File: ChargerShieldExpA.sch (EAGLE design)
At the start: 104 parts, among them IC1 TL431, IC2 LM324N, Q1 BUZ11, Q2 BD648, Q3 BUZ171, Q4 IRFZ48Z, T1 BC548, X1 +Vin, X2 VCC, X3 Battery

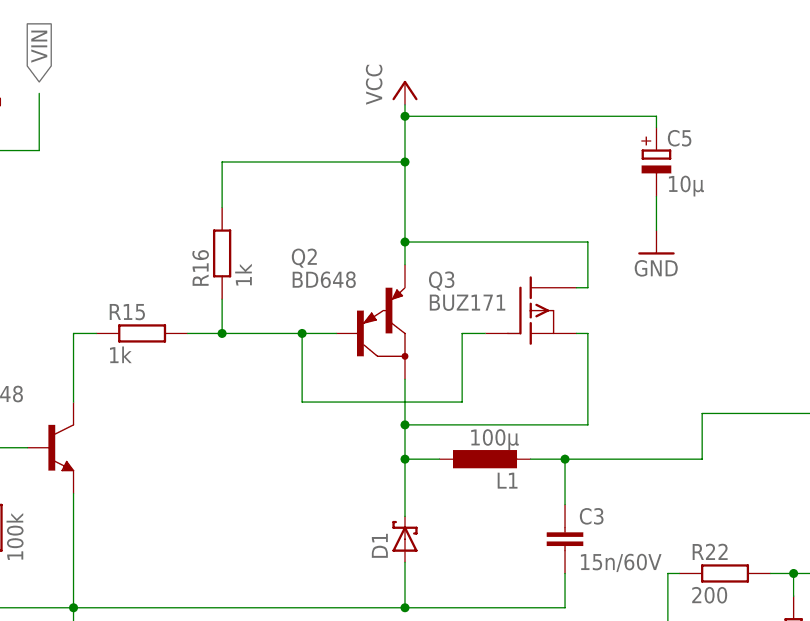
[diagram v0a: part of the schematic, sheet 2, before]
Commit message: - PROTOTYPE_BOARD define for prototype board use. - wrong FET connections
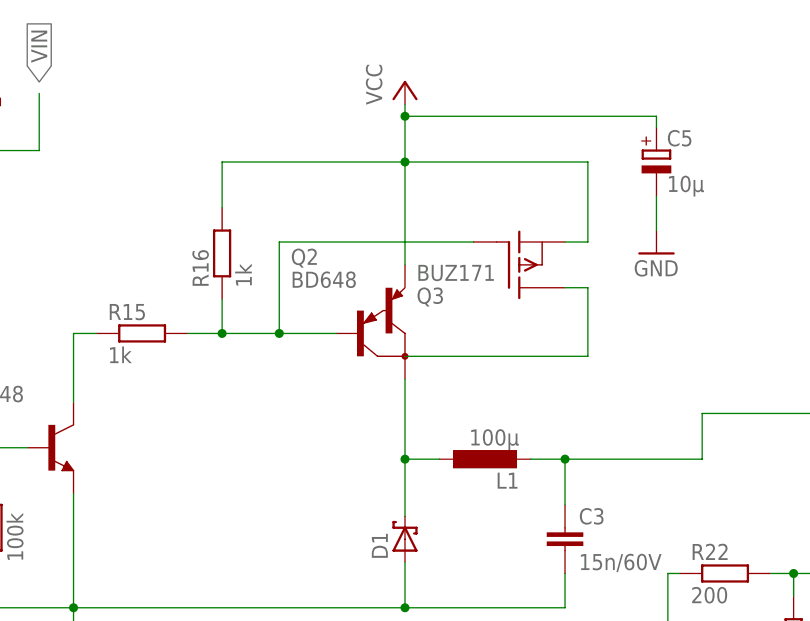
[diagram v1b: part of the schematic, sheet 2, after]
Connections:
- new net N$66: Q3.D
- net N$9: no longer Q3.S
- net VCC: now also Q3.S; no longer Q3.D
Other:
- moved on the sheet: Q3
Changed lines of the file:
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@@
 <instance part="R14" gate="G$1" x="66.04" y="57.15" rot="MR0"/>
 <instance part="C2" gate="G$1" x="72.39" y="40.64"/>
-<instance part="Q3" gate="G$1" x="113.03" y="140.97"/>
+<instance part="Q3" gate="G$1" x="111.76" y="146.05" rot="MR180"/>
 <instance part="JP8" gate="1" x="26.67" y="59.69"/>
 <instance part="JP18" gate="A" x="245.11" y="143.51"/>
@@
 <wire x1="78.74" y1="138.43" x2="78.74" y2="142.24" width="0.1524" layer="91"/>
 <pinref part="Q2" gate="G$1" pin="B"/>
-<wire x1="78.74" y1="138.43" x2="87.63" y2="138.43" width="0.1524" layer="91"/>
+<wire x1="78.74" y1="138.43" x2="85.09" y2="138.43" width="0.1524" layer="91"/>
 <junction x="78.74" y="138.43"/>
-<wire x1="87.63" y1="138.43" x2="91.44" y2="138.43" width="0.1524" layer="91"/>
-<wire x1="87.63" y1="138.43" x2="87.63" y2="130.81" width="0.1524" layer="91"/>
-<junction x="87.63" y="138.43"/>
-<wire x1="87.63" y1="130.81" x2="105.41" y2="130.81" width="0.1524" layer="91"/>
-<wire x1="105.41" y1="130.81" x2="105.41" y2="138.43" width="0.1524" layer="91"/>
+<wire x1="85.09" y1="138.43" x2="91.44" y2="138.43" width="0.1524" layer="91"/>
+<wire x1="85.09" y1="138.43" x2="85.09" y2="148.59" width="0.1524" layer="91"/>
+<junction x="85.09" y="138.43"/>
+<wire x1="85.09" y1="148.59" x2="106.68" y2="148.59" width="0.1524" layer="91"/>
 <pinref part="Q3" gate="G$1" pin="G"/>
-<wire x1="105.41" y1="138.43" x2="107.95" y2="138.43" width="0.1524" layer="91"/>
 </segment>
 </net>
@@
 <pinref part="Q2" gate="G$1" pin="E"/>
 <wire x1="99.06" y1="162.56" x2="99.06" y2="163.83" width="0.1524" layer="91"/>
-<wire x1="99.06" y1="146.05" x2="99.06" y2="148.59" width="0.1524" layer="91"/>
 <junction x="99.06" y="157.48"/>
-<pinref part="Q3" gate="G$1" pin="D"/>
-<wire x1="99.06" y1="148.59" x2="99.06" y2="157.48" width="0.1524" layer="91"/>
-<wire x1="118.11" y1="143.51" x2="119.38" y2="143.51" width="0.1524" layer="91"/>
-<wire x1="119.38" y1="143.51" x2="119.38" y2="148.59" width="0.1524" layer="91"/>
-<wire x1="119.38" y1="148.59" x2="99.06" y2="148.59" width="0.1524" layer="91"/>
-<junction x="99.06" y="148.59"/>
+<wire x1="99.06" y1="146.05" x2="99.06" y2="157.48" width="0.1524" layer="91"/>
 <pinref part="C5" gate="G$1" pin="+"/>
 <wire x1="99.06" y1="162.56" x2="127" y2="162.56" width="0.1524" layer="91"/>
 <wire x1="127" y1="162.56" x2="127" y2="161.29" width="0.1524" layer="91"/>
 <junction x="99.06" y="162.56"/>
+<pinref part="Q3" gate="G$1" pin="S"/>
+<wire x1="116.84" y1="148.59" x2="119.38" y2="148.59" width="0.1524" layer="91"/>
+<wire x1="119.38" y1="148.59" x2="119.38" y2="157.48" width="0.1524" layer="91"/>
+<wire x1="119.38" y1="157.48" x2="99.06" y2="157.48" width="0.1524" layer="91"/>
 </segment>
 <segment>
@@
 <wire x1="99.06" y1="118.11" x2="99.06" y2="124.46" width="0.1524" layer="91"/>
 <pinref part="L1" gate="G$1" pin="1"/>
-<wire x1="99.06" y1="124.46" x2="99.06" y2="128.27" width="0.1524" layer="91"/>
-<wire x1="99.06" y1="128.27" x2="99.06" y2="133.35" width="0.1524" layer="91"/>
+<wire x1="99.06" y1="124.46" x2="99.06" y2="133.35" width="0.1524" layer="91"/>
 <wire x1="102.87" y1="124.46" x2="99.06" y2="124.46" width="0.1524" layer="91"/>
 <junction x="99.06" y="124.46"/>
-<pinref part="Q3" gate="G$1" pin="S"/>
-<wire x1="118.11" y1="138.43" x2="119.38" y2="138.43" width="0.1524" layer="91"/>
-<wire x1="119.38" y1="138.43" x2="119.38" y2="128.27" width="0.1524" layer="91"/>
-<wire x1="119.38" y1="128.27" x2="99.06" y2="128.27" width="0.1524" layer="91"/>
-<junction x="99.06" y="128.27"/>
 </segment>
 </net>
@@
 </segment>
 </net>
+<net name="N$66" class="0">
+<segment>
+<wire x1="99.06" y1="135.89" x2="119.38" y2="135.89" width="0.1524" layer="91"/>
+<wire x1="119.38" y1="135.89" x2="119.38" y2="143.51" width="0.1524" layer="91"/>
+<pinref part="Q3" gate="G$1" pin="D"/>
+<wire x1="119.38" y1="143.51" x2="116.84" y2="143.51" width="0.1524" layer="91"/>
+</segment>
+</net>

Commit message: Higher input impedance for U_Batt
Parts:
- added R40: 1M, rcl:R-EU_0207/10
- C7: value 10µ -> 100n
- LED3: value (none) -> DIS1
- LED4: value (none) -> DIS2
- R11: value 1k -> 800
- R29: value 1k -> 100k
- R30: value 100k -> 10M
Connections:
- net GND: now also R40.1
- net N$18: now also R40.2
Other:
- note added: "*100k"
- note added: "*10µ"
- note added: "*1k"
- moved on the sheet: Q1, R11
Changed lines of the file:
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@@
 <part name="D2" library="diode" deviceset="1N4004" device=""/>
 <part name="JP13" library="bigger" deviceset="JP1E" device=""/>
-<part name="R29" library="rcl" deviceset="R-EU_" device="0207/12" value="1k"/>
+<part name="R29" library="rcl" deviceset="R-EU_" device="0207/12" value="100k"/>
 <part name="GND6" library="supply1" deviceset="GND" device=""/>
 <part name="GND7" library="supply1" deviceset="GND" device=""/>
@@
 <part name="R13" library="rcl" deviceset="R-EU_" device="0207/10" value="100k"/>
 <part name="R21" library="rcl" deviceset="R-EU_" device="0204/7" value="1k"/>
-<part name="R30" library="rcl" deviceset="R-EU_" device="0207/10" value="100k"/>
-<part name="C7" library="rcl" deviceset="CPOL-EU" device="E5-5" value="10µ"/>
+<part name="R30" library="rcl" deviceset="R-EU_" device="0207/10" value="10M"/>
+<part name="C7" library="rcl" deviceset="CPOL-EU" device="E5-5" value="100n"/>
 <part name="R27" library="rcl" deviceset="R-EU_" device="0207/10" value="10k"/>
 <part name="C4" library="rcl" deviceset="CPOL-EU" device="E5-5" value="3µ3"/>
@@
 <part name="P+5" library="supply1" deviceset="VCC" device=""/>
 <part name="GND12" library="supply1" deviceset="GND" device=""/>
-<part name="R11" library="rcl" deviceset="R-EU_" device="0204/7" value="1k"/>
+<part name="R11" library="rcl" deviceset="R-EU_" device="0204/7" value="800"/>
 <part name="R6" library="rcl" deviceset="R-EU_" device="0207/10" value="470"/>
-<part name="LED3" library="bigger" deviceset="LED" device="5MM_BIG"/>
+<part name="LED3" library="bigger" deviceset="LED" device="5MM_BIG" value="DIS1"/>
 <part name="P+6" library="supply1" deviceset="+5V" device=""/>
 <part name="S3" library="bigger" deviceset="SWITCH-MOMENTARY-2" device="PTH_UMSE" value="Start"/>
@@
 <part name="R2" library="rcl" deviceset="R-EU_" device="0207/10" value="4k7"/>
 <part name="R7" library="rcl" deviceset="R-EU_" device="0207/10" value="470"/>
-<part name="LED4" library="bigger" deviceset="LED" device="5MM_BIG"/>
+<part name="LED4" library="bigger" deviceset="LED" device="5MM_BIG" value="DIS2"/>
 <part name="R14" library="rcl" deviceset="R-EU_" device="0207/10" value="0"/>
 <part name="C2" library="rcl" deviceset="CPOL-EU" device="E5-5" value="3µ3"/>
@@
 <part name="R39" library="rcl" deviceset="R-EU_" device="0204/7" value="*"/>
 <part name="JP25" library="bigger" deviceset="JP1E" device=""/>
+<part name="R40" library="rcl" deviceset="R-EU_" device="0207/10" value="1M"/>
 </parts>
 <sheets>
@@
 Voltage</text>
 <text x="234.95" y="6.35" size="2.54" layer="105">by Jedzia</text>
+<text x="217.805" y="135.255" size="1.778" layer="96">*1k</text>
+<text x="229.87" y="127.635" size="1.778" layer="96">*10µ</text>
+<text x="245.11" y="129.54" size="1.778" layer="96" rot="R90">*100k</text>
 </plain>
 <instances>
@@
 <instance part="P+5" gate="VCC" x="16.51" y="64.77"/>
 <instance part="GND12" gate="1" x="26.67" y="19.05"/>
-<instance part="R11" gate="G$1" x="49.53" y="72.39"/>
-<instance part="Q1" gate="G$1" x="62.23" y="74.93"/>
+<instance part="R11" gate="G$1" x="36.83" y="72.39"/>
+<instance part="Q1" gate="G$1" x="50.8" y="74.93"/>
 <instance part="P+7" gate="1" x="34.29" y="64.77"/>
 <instance part="R14" gate="G$1" x="66.04" y="57.15" rot="MR0"/>
@@
 <instance part="JP16" gate="A" x="236.22" y="100.33"/>
 <instance part="R39" gate="G$1" x="134.62" y="72.39" rot="R90"/>
+<instance part="R40" gate="G$1" x="43.18" y="40.64" rot="R90"/>
 </instances>
 <busses>
@@
 <wire x1="72.39" y1="22.86" x2="58.42" y2="22.86" width="0.1524" layer="91"/>
 <junction x="58.42" y="22.86"/>
+<pinref part="R40" gate="G$1" pin="1"/>
+<wire x1="43.18" y1="35.56" x2="43.18" y2="22.86" width="0.1524" layer="91"/>
+<wire x1="43.18" y1="22.86" x2="52.07" y2="22.86" width="0.1524" layer="91"/>
+<junction x="52.07" y="22.86"/>
 </segment>
 <segment>
@@
 <junction x="210.82" y="107.95"/>
 <wire x1="180.34" y1="107.95" x2="180.34" y2="91.44" width="0.1524" layer="91"/>
-<wire x1="180.34" y1="91.44" x2="68.58" y2="91.44" width="0.1524" layer="91"/>
-<wire x1="68.58" y1="77.47" x2="68.58" y2="91.44" width="0.1524" layer="91"/>
+<wire x1="180.34" y1="91.44" x2="57.15" y2="91.44" width="0.1524" layer="91"/>
+<wire x1="57.15" y1="77.47" x2="57.15" y2="91.44" width="0.1524" layer="91"/>
 <pinref part="Q1" gate="G$1" pin="D"/>
-<wire x1="68.58" y1="77.47" x2="67.31" y2="77.47" width="0.1524" layer="91"/>
+<wire x1="57.15" y1="77.47" x2="55.88" y2="77.47" width="0.1524" layer="91"/>
 </segment>
 </net>
@@
 <pinref part="Q1" gate="G$1" pin="G"/>
 <pinref part="R11" gate="G$1" pin="2"/>
-<wire x1="57.15" y1="72.39" x2="54.61" y2="72.39" width="0.1524" layer="91"/>
+<wire x1="45.72" y1="72.39" x2="43.18" y2="72.39" width="0.1524" layer="91"/>
+<pinref part="R40" gate="G$1" pin="2"/>
+<wire x1="43.18" y1="72.39" x2="41.91" y2="72.39" width="0.1524" layer="91"/>
+<wire x1="43.18" y1="45.72" x2="43.18" y2="72.39" width="0.1524" layer="91"/>
+<junction x="43.18" y="72.39"/>
 </segment>
 </net>
@@
 <segment>
 <pinref part="R11" gate="G$1" pin="1"/>
-<wire x1="44.45" y1="72.39" x2="40.64" y2="72.39" width="0.1524" layer="91"/>
-<wire x1="40.64" y1="72.39" x2="40.64" y2="83.82" width="0.1524" layer="91"/>
-<wire x1="40.64" y1="83.82" x2="54.61" y2="83.82" width="0.1524" layer="91"/>
-<wire x1="54.61" y1="83.82" x2="54.61" y2="88.9" width="0.1524" layer="91"/>
-<wire x1="54.61" y1="88.9" x2="49.53" y2="88.9" width="0.1524" layer="91"/>
-<label x="49.53" y="88.9" size="2.54" layer="95" rot="R180" xref="yes"/>
+<wire x1="31.75" y1="72.39" x2="27.94" y2="72.39" width="0.1524" layer="91"/>
+<wire x1="27.94" y1="72.39" x2="27.94" y2="90.17" width="0.1524" layer="91"/>
+<label x="27.94" y="90.17" size="1.6764" layer="95" rot="R90" xref="yes"/>
 </segment>
 </net>
@@
 <segment>
 <wire x1="55.88" y1="57.15" x2="52.07" y2="57.15" width="0.1524" layer="91"/>
-<wire x1="69.85" y1="72.39" x2="69.85" y2="63.5" width="0.1524" layer="91"/>
-<wire x1="69.85" y1="63.5" x2="52.07" y2="63.5" width="0.1524" layer="91"/>
+<wire x1="57.15" y1="72.39" x2="57.15" y2="63.5" width="0.1524" layer="91"/>
+<wire x1="57.15" y1="63.5" x2="52.07" y2="63.5" width="0.1524" layer="91"/>
 <wire x1="52.07" y1="63.5" x2="52.07" y2="57.15" width="0.1524" layer="91"/>
 <pinref part="R12" gate="G$1" pin="1"/>
@@
 <junction x="52.07" y="57.15"/>
 <pinref part="Q1" gate="G$1" pin="S"/>
-<wire x1="67.31" y1="72.39" x2="69.85" y2="72.39" width="0.1524" layer="91"/>
+<wire x1="55.88" y1="72.39" x2="57.15" y2="72.39" width="0.1524" layer="91"/>
 <pinref part="JP10" gate="A" pin="1"/>
 </segment>
